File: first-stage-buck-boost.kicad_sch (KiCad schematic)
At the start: 17 parts, among them U7 TPS5516x-Q1

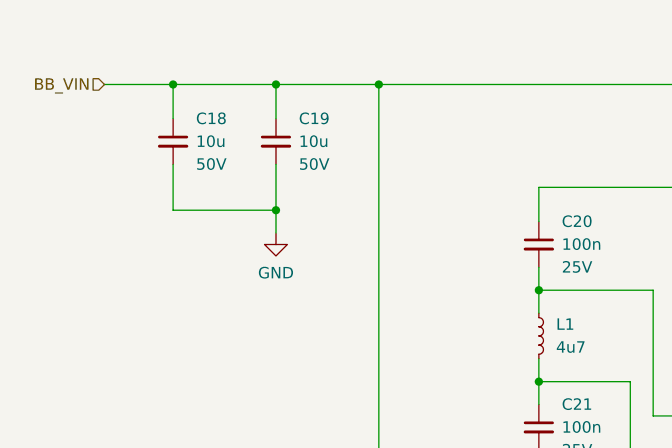
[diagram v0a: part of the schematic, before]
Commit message: Update tolerances, finish BOM
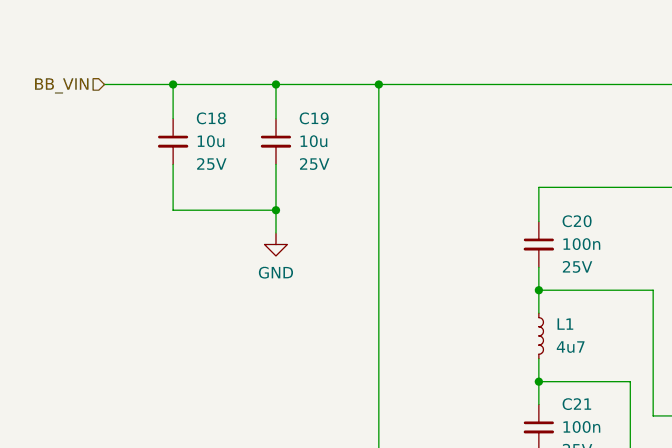
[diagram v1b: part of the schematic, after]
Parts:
- C18, C19: Rating 50V -> 25V
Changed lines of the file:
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@@
       (effects (font (size 1.27 1.27)) hide)
     )
-    (property "Rating" "50V" (id 4) (at 50.8 58.4138 0)
+    (property "Rating" "25V" (id 4) (at 50.8 58.4138 0)
       (effects (font (size 1.27 1.27)) (justify left))
     )
@@
       (effects (font (size 1.27 1.27)) hide)
     )
-    (property "Rating" "50V" (id 4) (at 39.37 58.4138 0)
+    (property "Rating" "25V" (id 4) (at 39.37 58.4138 0)
       (effects (font (size 1.27 1.27)) (justify left))
     )
